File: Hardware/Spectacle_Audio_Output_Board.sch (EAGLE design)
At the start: 86 parts, among them J4 AUDIO-JACK3, J5 AUDIO-JACK3, U1 CY8C4146LQI-S422, U2 3.3V, U3 3.3V, U4 AT25SF041-SOIC8, U5 VS1000, Y1 12MHz

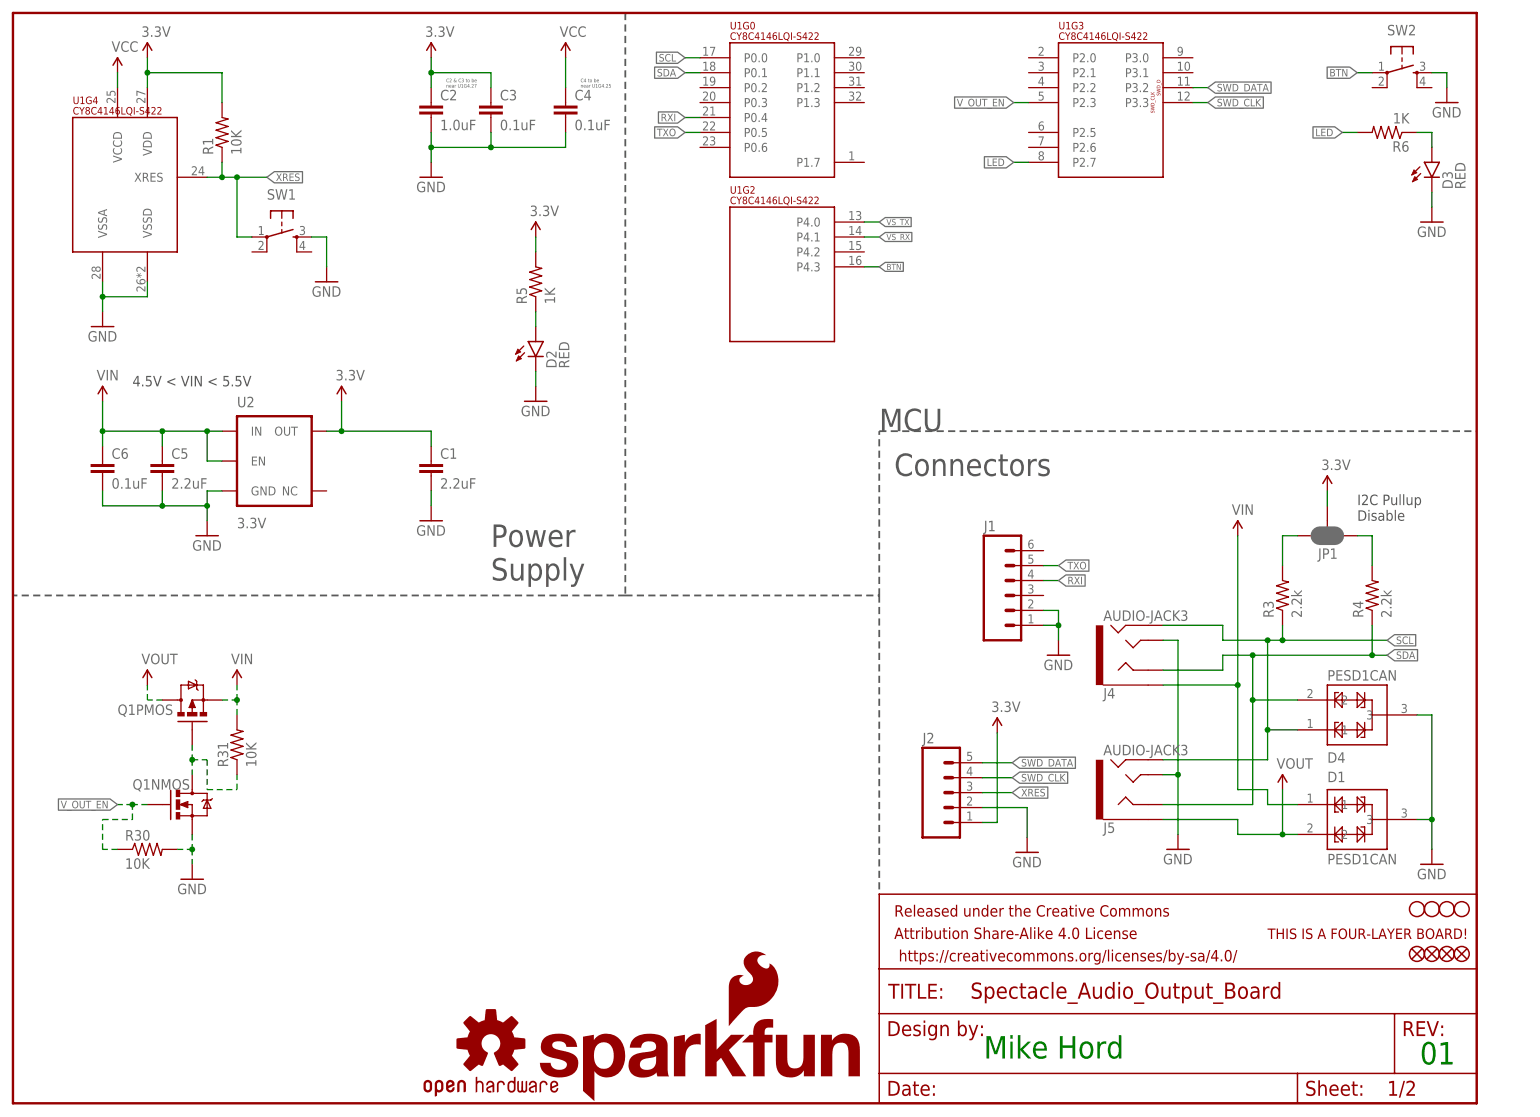
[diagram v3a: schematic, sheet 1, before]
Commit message: Change pullup resistor values to 4.7k Add firmware to repo
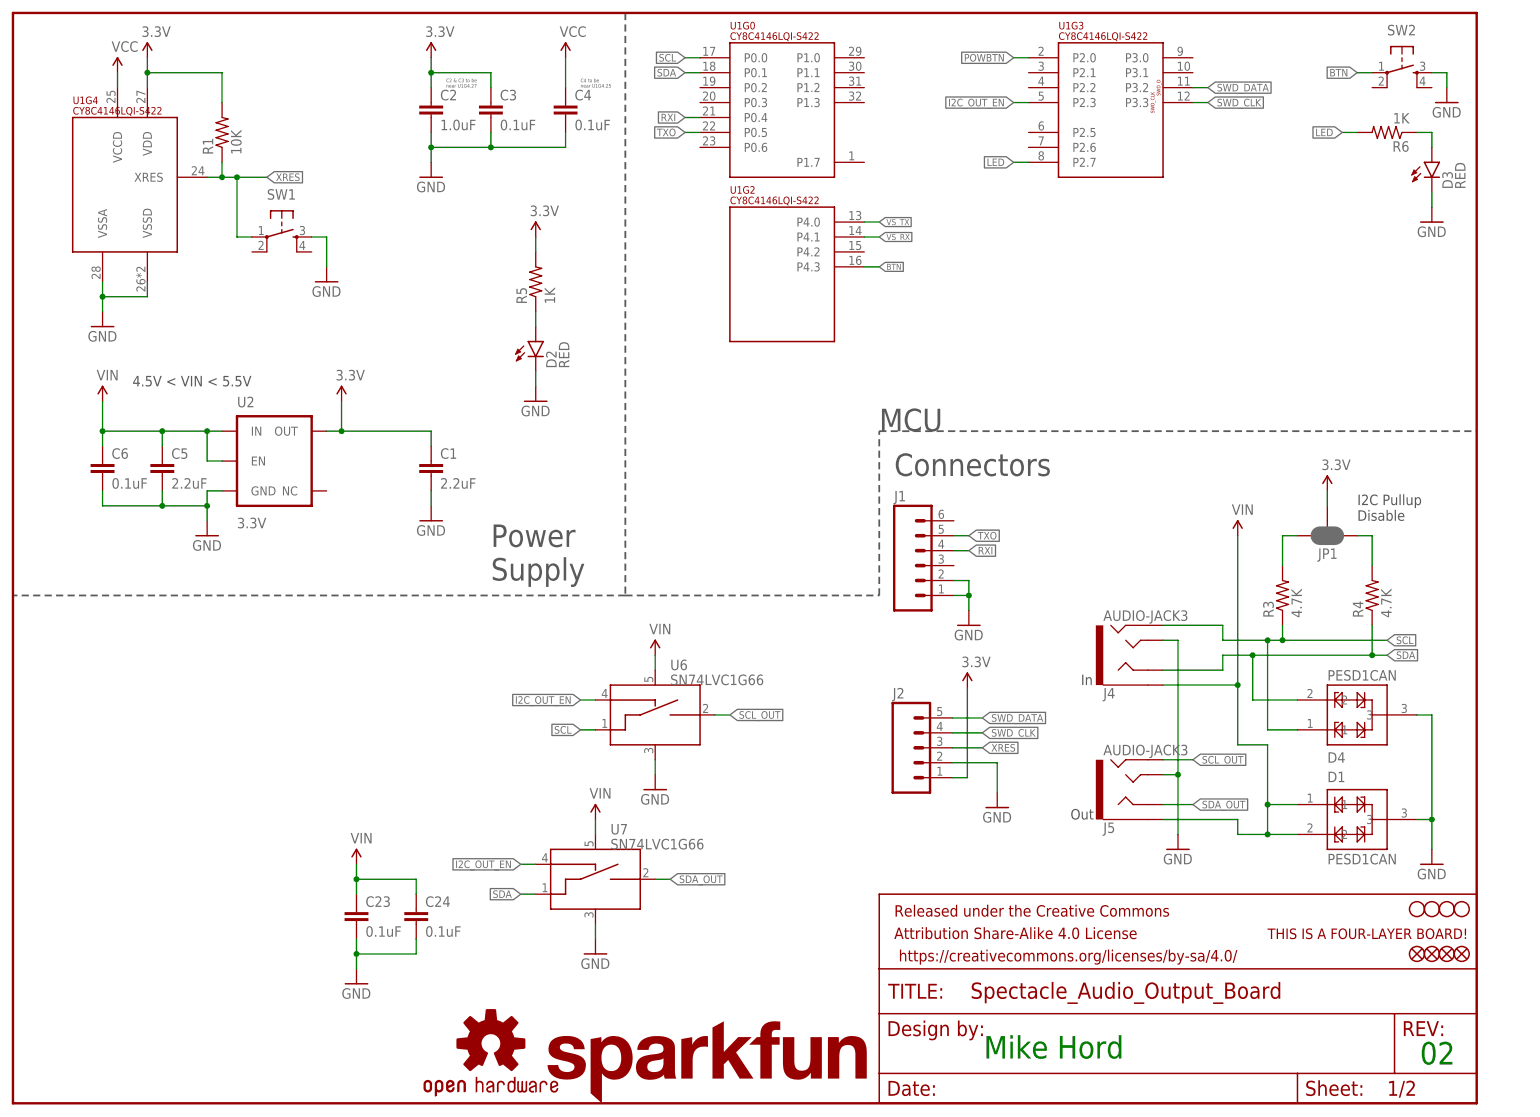
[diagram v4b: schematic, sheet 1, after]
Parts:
- removed C21: 1.0uF, SparkFun-Capacitors:1.0UF-16V-10%(0402)
- removed Q1: (no value), SparkFun-DiscreteSemi:IRF7509
- removed R30, R31: 10K, SparkFun-Resistors:10KOHM-1/10W-1%(0603)0603
- added C23, C24: 0.1uF, SparkFun-Capacitors:0.1UF-16V(+-10%)(0402)
- added U6, U7: SN74LVC1G66, SparkFun-AnalogIC:SN74LVC1G66_SPST_AMUX
- J2: device SparkFun-Connectors:M05PTH -> SparkFun-Connectors:M05NO_SILK
- LOGO2: value SFE_LOGO_NAME_FLAME.1_INCH -> SFE_LOGO_NAME.1_INCH; device SparkFun-Aesthetics:SFE_LOGO_NAME_FLAME.1_INCH -> SparkFun-Aesthetics:SFE_LOGO_NAME.1_INCH
- R3, R4: value 2.2k -> 4.7K; device SparkFun-Resistors:2.2KOHM-1/10W-1%(0603) -> SparkFun-Resistors:4.7KOHM-1/10W-1%(0603)
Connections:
- removed net N$15: C21.1, R26.1, U5.POWBTN
- removed net N$26: Q1NMOS.D, Q1PMOS.G, R31.1
- removed net VOUT: D1.2, J5.EARTH, Q1PMOS.D
- removed net V_OUT_EN: Q1NMOS.G, R30.1, U1G3.P2.3
- new net I2C_OUT_EN: U1G3.P2.3, U6.CTRL_IN, U7.CTRL_IN
- new net POWBTN: R26.1, U1G3.P2.0, U5.POWBTN
- new net SCL_OUT: J5.RING2, U6.A_OUT
- new net SDA_OUT: J5.RING1, U7.A_OUT
- net 3.3V: no longer C21.2
- net GND: now also C23.2, C24.2, U6.VSS, U7.VSS; no longer Q1NMOS.S, R30.2
- net SCL: now also U6.A_IN; no longer J5.RING2
- net SDA: now also U7.A_IN; no longer J5.RING1
- net VIN: now also C23.1, C24.1, D1.2, J5.EARTH, U6.VCC, U7.VCC; no longer Q1PMOS.S, R31.2
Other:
- note added: "02"
- note added: "In"
- note added: "Out"
- moved on the sheet: C20, J1, J2, U3

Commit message: Changes from review/checklist
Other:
- note removed: "01"
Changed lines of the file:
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@@
 <wire x1="104.14" y1="86.36" x2="0" y2="86.36" width="0.3048" layer="97" style="longdash"/>
 <wire x1="104.14" y1="86.36" x2="147.32" y2="86.36" width="0.3048" layer="97" style="longdash"/>
-<text x="165.1" y="7.62" size="3.81" layer="91" font="vector">Mike Hord</text>
-<text x="239.268" y="6.604" size="3.81" layer="91" font="vector">02</text>
+<text x="165.1" y="7.62" size="3.81" layer="94" font="vector">Mike Hord</text>
+<text x="239.268" y="6.604" size="3.81" layer="94" font="vector">02</text>
 <wire x1="147.32" y1="86.36" x2="147.32" y2="114.3" width="0.3048" layer="97" style="longdash"/>
 <wire x1="147.32" y1="114.3" x2="248.92" y2="114.3" width="0.3048" layer="97" style="longdash"/>
@@
 <text x="94.488" y="46.99" size="2.54" layer="97" font="vector">Audio signal decoupling</text>
 <text x="2.54" y="180.34" size="2.54" layer="97" font="vector">VS1000 Codec</text>
-<text x="165.1" y="7.62" size="3.81" layer="91" font="vector">Mike Hord</text>
-<text x="239.268" y="6.604" size="3.81" layer="91" font="vector">01</text>
+<text x="165.1" y="7.62" size="3.81" layer="94" font="vector">Mike Hord</text>
+<text x="239.268" y="6.604" size="3.81" layer="94" font="vector">02</text>
 </plain>
 <instances>

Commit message: Fixes from review
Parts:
- J1: device SparkFun-Connectors:M06NO_SILK_FEMALE_PTH -> SparkFun-Connectors:M06NO_SILK_NO_POP
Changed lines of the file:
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@@
 <grid distance="0.1" unitdist="inch" unit="inch" style="lines" multiple="1" display="no" altdistance="0.01" altunitdist="inch" altunit="inch"/>
 <layers>
-<layer number="1" name="Top" color="4" fill="1" visible="no" active="no"/>
-<layer number="2" name="Route2" color="1" fill="3" visible="no" active="no"/>
-<layer number="3" name="Route3" color="4" fill="3" visible="no" active="no"/>
-<layer number="4" name="Route4" color="1" fill="4" visible="no" active="no"/>
-<layer number="5" name="Route5" color="4" fill="4" visible="no" active="no"/>
-<layer number="6" name="Route6" color="1" fill="8" visible="no" active="no"/>
-<layer number="7" name="Route7" color="4" fill="8" visible="no" active="no"/>
-<layer number="8" name="Route8" color="1" fill="2" visible="no" active="no"/>
-<layer number="9" name="Route9" color="4" fill="2" visible="no" active="no"/>
-<layer number="10" name="Route10" color="1" fill="7" visible="no" active="no"/>
-<layer number="11" name="Route11" color="4" fill="7" visible="no" active="no"/>
-<layer number="12" name="Route12" color="1" fill="5" visible="no" active="no"/>
-<layer number="13" name="Route13" color="4" fill="5" visible="no" active="no"/>
-<layer number="14" name="Route14" color="1" fill="6" visible="no" active="no"/>
-<layer number="15" name="Route15" color="4" fill="6" visible="no" active="no"/>
-<layer number="16" name="Bottom" color="1" fill="1" visible="no" active="no"/>
-<layer number="17" name="Pads" color="2" fill="1" visible="no" active="no"/>
-<layer number="18" name="Vias" color="2" fill="1" visible="no" active="no"/>
-<layer number="19" name="Unrouted" color="6" fill="1" visible="no" active="no"/>
-<layer number="20" name="Dimension" color="15" fill="1" visible="no" active="no"/>
-<layer number="21" name="tPlace" color="16" fill="1" visible="no" active="no"/>
-<layer number="22" name="bPlace" color="14" fill="1" visible="no" active="no"/>
-<layer number="23" name="tOrigins" color="15" fill="1" visible="no" active="no"/>
-<layer number="24" name="bOrigins" color="15" fill="1" visible="no" active="no"/>
-<layer number="25" name="tNames" color="7" fill="1" visible="no" active="no"/>
-<layer number="26" name="bNames" color="7" fill="1" visible="no" active="no"/>
-<layer number="27" name="tValues" color="7" fill="1" visible="no" active="no"/>
-<layer number="28" name="bValues" color="7" fill="1" visible="no" active="no"/>
+<layer number="1" name="Top" color="4" fill="1" visible="yes" active="no"/>
+<layer number="2" name="Route2" color="1" fill="3" visible="yes" active="no"/>
+<layer number="3" name="Route3" color="4" fill="3" visible="yes" active="no"/>
+<layer number="4" name="Route4" color="1" fill="4" visible="yes" active="no"/>
+<layer number="5" name="Route5" color="4" fill="4" visible="yes" active="no"/>
+<layer number="6" name="Route6" color="1" fill="8" visible="yes" active="no"/>
+<layer number="7" name="Route7" color="4" fill="8" visible="yes" active="no"/>
+<layer number="8" name="Route8" color="1" fill="2" visible="yes" active="no"/>
+<layer number="9" name="Route9" color="4" fill="2" visible="yes" active="no"/>
+<layer number="10" name="Route10" color="1" fill="7" visible="yes" active="no"/>
+<layer number="11" name="Route11" color="4" fill="7" visible="yes" active="no"/>
+<layer number="12" name="Route12" color="1" fill="5" visible="yes" active="no"/>
+<layer number="13" name="Route13" color="4" fill="5" visible="yes" active="no"/>
+<layer number="14" name="Route14" color="1" fill="6" visible="yes" active="no"/>
+<layer number="15" name="Route15" color="4" fill="6" visible="yes" active="no"/>
+<layer number="16" name="Bottom" color="1" fill="1" visible="yes" active="no"/>
+<layer number="17" name="Pads" color="2" fill="1" visible="yes" active="no"/>
+<layer number="18" name="Vias" color="2" fill="1" visible="yes" active="no"/>
+<layer number="19" name="Unrouted" color="6" fill="1" visible="yes" active="no"/>
+<layer number="20" name="Dimension" color="15" fill="1" visible="yes" active="no"/>
+<layer number="21" name="tPlace" color="16" fill="1" visible="yes" active="no"/>
+<layer number="22" name="bPlace" color="14" fill="1" visible="yes" active="no"/>
+<layer number="23" name="tOrigins" color="15" fill="1" visible="yes" active="no"/>
+<layer number="24" name="bOrigins" color="15" fill="1" visible="yes" active="no"/>
+<layer number="25" name="tNames" color="7" fill="1" visible="yes" active="no"/>
+<layer number="26" name="bNames" color="7" fill="1" visible="yes" active="no"/>
+<layer number="27" name="tValues" color="7" fill="1" visible="yes" active="no"/>
+<layer number="28" name="bValues" color="7" fill="1" visible="yes" active="no"/>
 <layer number="29" name="tStop" color="7" fill="3" visible="no" active="no"/>
 <layer number="30" name="bStop" color="7" fill="6" visible="no" active="no"/>
@@
 <layer number="35" name="tGlue" color="7" fill="4" visible="no" active="no"/>
 <layer number="36" name="bGlue" color="7" fill="5" visible="no" active="no"/>
-<layer number="37" name="tTest" color="7" fill="1" visible="no" active="no"/>
-<layer number="38" name="bTest" color="7" fill="1" visible="no" active="no"/>
+<layer number="37" name="tTest" color="7" fill="1" visible="yes" active="no"/>
+<layer number="38" name="bTest" color="7" fill="1" visible="yes" active="no"/>
 <layer number="39" name="tKeepout" color="4" fill="11" visible="no" active="no"/>
 <layer number="40" name="bKeepout" color="1" fill="11" visible="no" active="no"/>
@@
 <layer number="44" name="Drills" color="7" fill="1" visible="no" active="no"/>
 <layer number="45" name="Holes" color="7" fill="1" visible="no" active="no"/>
-<layer number="46" name="Milling" color="3" fill="1" visible="no" active="no"/>
-<layer number="47" name="Measures" color="7" fill="1" visible="no" active="no"/>
-<layer number="48" name="Document" color="7" fill="1" visible="no" active="no"/>
-<layer number="49" name="Reference" color="7" fill="1" visible="no" active="no"/>
-<layer number="50" name="dxf" color="7" fill="1" visible="no" active="no"/>
-<layer number="51" name="tDocu" color="6" fill="1" visible="no" active="no"/>
-<layer number="52" name="bDocu" color="7" fill="1" visible="no" active="no"/>
-<layer number="53" name="tGND_GNDA" color="7" fill="9" visible="no" active="no"/>
-<layer number="54" name="bGND_GNDA" color="1" fill="9" visible="no" active="no"/>
-<layer number="56" name="wert" color="7" fill="1" visible="no" active="no"/>
-<layer number="57" name="tCAD" color="7" fill="1" visible="no" active="no"/>
-<layer number="59" name="tCarbon" color="7" fill="1" visible="no" active="no"/>
-<layer number="60" name="bCarbon" color="7" fill="1" visible="no" active="no"/>
+<layer number="46" name="Milling" color="3" fill="1" visible="yes" active="no"/>
+<layer number="47" name="Measures" color="7" fill="1" visible="yes" active="no"/>
+<layer number="48" name="Document" color="7" fill="1" visible="yes" active="no"/>
+<layer number="49" name="Reference" color="7" fill="1" visible="yes" active="no"/>
+<layer number="50" name="dxf" color="7" fill="1" visible="yes" active="no"/>
+<layer number="51" name="tDocu" color="6" fill="1" visible="yes" active="no"/>
+<layer number="52" name="bDocu" color="7" fill="1" visible="yes" active="no"/>
+<layer number="53" name="tGND_GNDA" color="7" fill="9" visible="yes" active="no"/>
+<layer number="54" name="bGND_GNDA" color="1" fill="9" visible="yes" active="no"/>
+<layer number="56" name="wert" color="7" fill="1" visible="yes" active="no"/>
+<layer number="57" name="tCAD" color="7" fill="1" visible="yes" active="no"/>
+<layer number="59" name="tCarbon" color="7" fill="1" visible="yes" active="no"/>
+<layer number="60" name="bCarbon" color="7" fill="1" visible="yes" active="no"/>
 <layer number="90" name="Modules" color="5" fill="1" visible="yes" active="yes"/>
 <layer number="91" name="Nets" color="2" fill="1" visible="yes" active="yes"/>
@@
 <part name="C17" library="SparkFun-Capacitors" deviceset="10UF-6.3V-20%(0603)" device="" value="10uF"/>
 <part name="J5" library="SparkFun-Connectors" deviceset="AUDIO-JACK3" device=""/>
-<part name="J1" library="SparkFun-Connectors" deviceset="M06" device="NO_SILK_FEMALE_PTH"/>
+<part name="J1" library="SparkFun-Connectors" deviceset="M06" device="NO_SILK_NO_POP"/>
 <part name="C19" library="SparkFun-Capacitors" deviceset="1.0UF-16V-10%(0402)" device="" value="1.0uF"/>
 <part name="GND20" library="SparkFun-Aesthetics" deviceset="GND" device=""/>
